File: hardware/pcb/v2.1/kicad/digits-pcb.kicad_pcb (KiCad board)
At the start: 2 copper layers, 61.9 x 76.2 mm, 77 parts, among them J1 Conn_02x20_Odd_Even, J3 VIN_BARREL_PIGTAIL, J4 Conn_01x07, J6 Conn_01x02, J7 Screw_Terminal_01x02, J8 Conn_01x04, SW1 Hook_DPDT, SW2 SW_Push, U10 XL6019E1, U2 DRV8871DDAR, U3 RP2040, U4 W25Q16JVSSIQ, U5 AMS1117-3.3, U6 TLV320AIC3104IRHBR, U7 XC6206P182MR, Y1 ABM8-272-T3

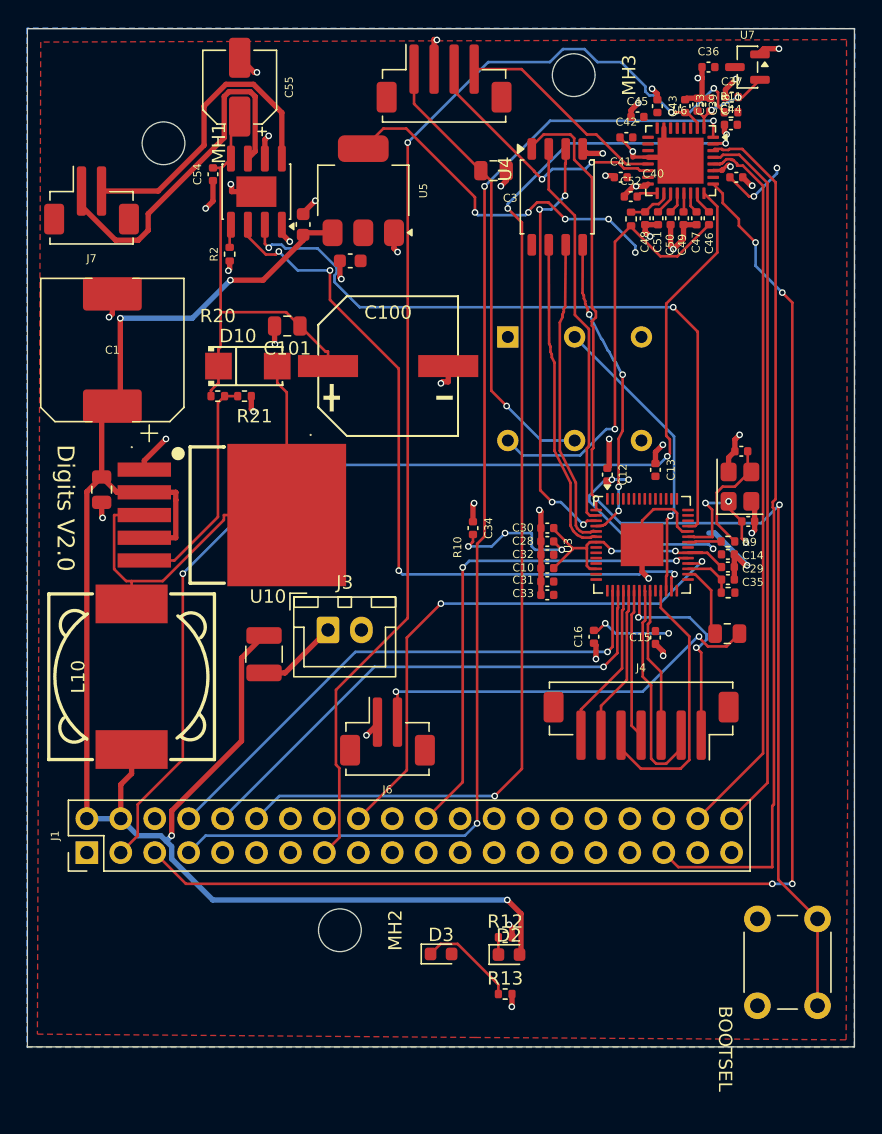
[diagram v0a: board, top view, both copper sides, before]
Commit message: fix(hardware): sync connector refs across sch/pcb, clean pre-fab defects
Rename connectors to semantic references in both schematic and PCB so the
two stay consistent: PWR, LED, KEYPAD, BELL, "Pi Zero W 2". Update the
baked unconnected-net placeholder names on the Pi header to match. Remove
a dangling via stub on the XIN crystal net, and add two GND vias to the
DRV8871 (U2) exposed pad for a lower-inductance ground tie.

DRC clean: 0 errors, 0 unconnected, 0 schematic-parity issues.
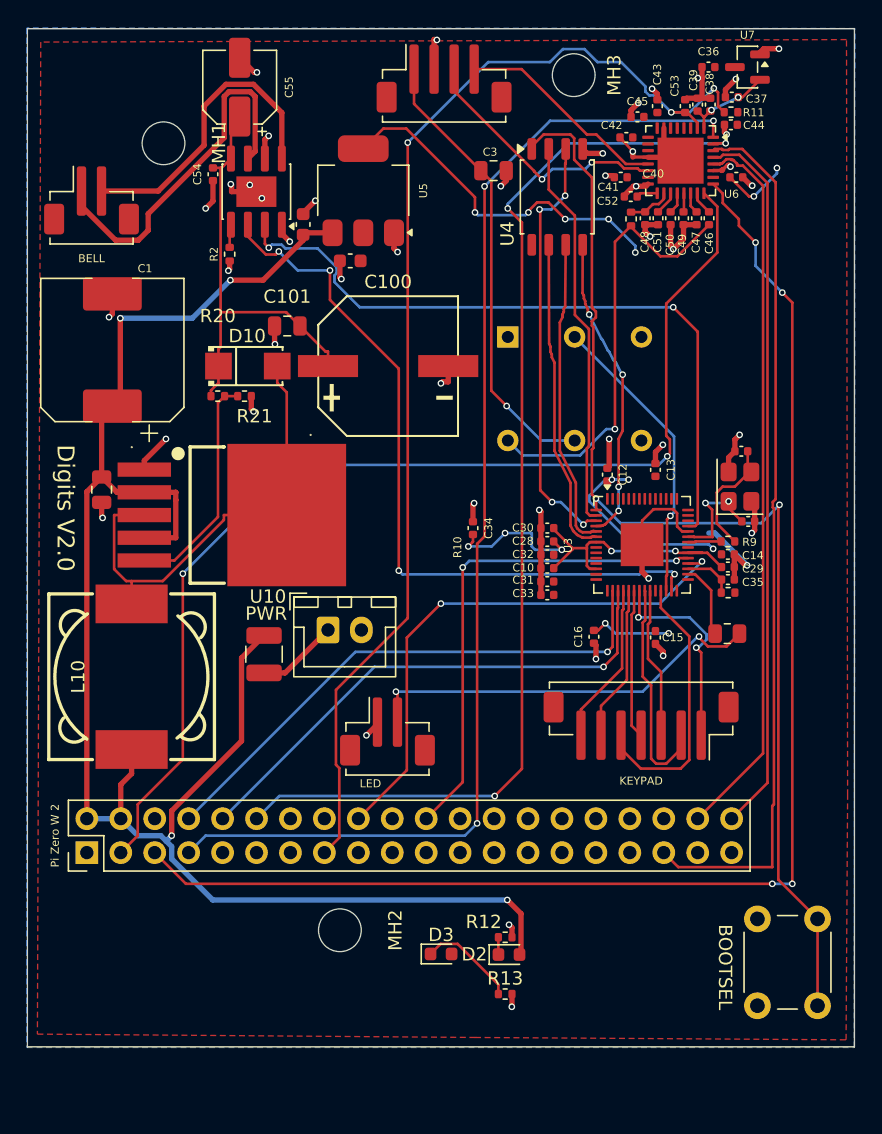
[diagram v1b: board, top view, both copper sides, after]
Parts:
- Pi Zero W 2: renamed from J1
- renumbered J7 to BELL, J4 to KEYPAD, J6 to LED, J3 to PWR
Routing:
- net XIN: track 10.0 -> 8.32 mm, vias 3 -> 2
- net GND: vias 44 -> 46
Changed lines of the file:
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@@
 		(tags "capacitor")
 		(property "Reference" "C41"
-			(at 0 1.16 0)
+			(at 0.934 -0.7327 0)
 			(layer "F.SilkS")
 			(effects
@@
 		(tags "capacitor electrolytic")
 		(property "Reference" "C1"
-			(at 0 0 0)
+			(at 6.0984 2.4411 0)
 			(layer "F.SilkS")
 			(effects
@@
 		(tags "capacitor")
 		(property "Reference" "C39"
-			(at 0 1.16 90)
+			(at 1.8319 -0.3115 90)
 			(layer "F.SilkS")
 			(effects
@@
 		(tags "capacitor")
 		(property "Reference" "C15"
-			(at 0 1.16 0)
+			(at 0 -1.2934 0)
 			(layer "F.SilkS")
 			(effects
@@
 		(tags "resistor")
 		(property "Reference" "R12"
-			(at 0 -1.17 0)
+			(at -1.61 -1.15 0)
 			(layer "F.SilkS")
 			(effects
@@
 		(tags "capacitor")
 		(property "Reference" "C101"
-			(at 0 -1.68 0)
+			(at 0 2.2 0)
 			(layer "F.SilkS")
 			(effects
@@
 		(tags "LED")
 		(property "Reference" "D2"
-			(at 0 -1.43 0)
+			(at -2.595 -0.02 0)
 			(layer "F.SilkS")
 			(effects
@@
 		(tags "capacitor")
 		(property "Reference" "C43"
-			(at 0 1.16 90)
+			(at 2.3696 -0.0021 90)
 			(layer "F.SilkS")
 			(effects
@@
 		(tags "mountinghole M3")
 		(property "Reference" "MH3"
-			(at 0 4.15 90)
+			(at 0 3.036 90)
 			(layer "F.SilkS")
 			(effects
@@
 		(tags "capacitor")
 		(property "Reference" "C44"
-			(at 0 1.16 0)
+			(at -1.7216 -0.0339 0)
 			(layer "F.SilkS")
 			(effects
@@
 		(tags "capacitor")
 		(property "Reference" "C42"
-			(at 0 1.16 0)
+			(at 1.1057 0.9148 0)
 			(layer "F.SilkS")
 			(effects
@@
 		(tags "Texas VQFN NoLead")
 		(property "Reference" "U6"
-			(at 0.0625 3.75 0)
+			(at -3.811 -2.4995 0)
 			(layer "F.SilkS")
 			(effects
@@
 		(tags "resistor")
 		(property "Reference" "R11"
-			(at 0 1.17 0)
+			(at -1.6879 -0.026 0)
 			(layer "F.SilkS")
 			(effects
@@
 		(descr "SS56")
 		(property "Reference" "D10"
-			(at -0.75 -2.25 0)
+			(at -0.05 -2.25 0)
 			(layer "F.SilkS")
 			(effects
@@
 		(tags "capacitor")
 		(property "Reference" "C3"
-			(at 1.25 2.05 0)
+			(at -0.264 -1.4005 0)
 			(layer "F.SilkS")
 			(effects
@@
 		(tags "SOIC SO P-SOP SOP SOP-8 SO SO-8 8S2 S2AE/F K04-056 CASE-751BE SO8W 8-Pin-SOIC PSA W8-2 W8-4 W8MS-1 FPT-8P-M08")
 		(property "Reference" "U4"
-			(at -2.0875 3.905 90)
+			(at 2.76 3.73 90)
 			(layer "F.SilkS")
 			(effects
@@
 		(descr "JST XH series connector, B2B-XH-A (http://www.jst-mfg.com/product/pdf/eng/eXH.pdf)")
 		(tags "connector JST XH vertical")
-		(property "Reference" "J3"
-			(at 1.25 -3.55 0)
+		(property "Reference" "PWR"
+			(at -4.625 -1.225 0)
 			(layer "F.SilkS")
 			(effects
@@
 		(tags "capacitor")
 		(property "Reference" "C53"
-			(at 0.112504 1.133301 90)
+			(at 1.5186 -0.7804 90)
 			(layer "F.SilkS")
 			(effects
@@
 		(tags "capacitor")
 		(property "Reference" "C38"
-			(at 0 1.16 90)
+			(at 1.5555 -0.0373 90)
 			(layer "F.SilkS")
 			(effects
@@
 		(descr "Through hole straight pin header, 2x20, 2.54mm pitch, double rows")
 		(tags "Through hole pin header THT 2x20 2.54mm double row")
-		(property "Reference" "J1"
+		(property "Reference" "Pi Zero W 2"
 			(at 1.27 -2.38 90)
 			(layer "F.SilkS")
@@
 			(layers "*.Cu" "*.Mask")
 			(remove_unused_layers no)
-			(net "unconnected-(J1-Pin_1-Pad1)")
+			(net "unconnected-(Pi Zero W 2-Pin_1-Pad1)")
 			(pinfunction "Pin_1_1")
 			(pintype "passive+no_connect")
@@
 			(layers "*.Cu" "*.Mask")
 			(remove_unused_layers no)
-			(net "unconnected-(J1-Pin_11-Pad11)")
+			(net "unconnected-(Pi Zero W 2-Pin_11-Pad11)")
 			(pinfunction "Pin_11_11")
 			(pintype "passive+no_connect")
@@
 			(layers "*.Cu" "*.Mask")
 			(remove_unused_layers no)
-			(net "unconnected-(J1-Pin_13-Pad13)")
+			(net "unconnected-(Pi Zero W 2-Pin_13-Pad13)")
 			(pinfunction "Pin_13_13")
 			(pintype "passive+no_connect")
@@
 			(layers "*.Cu" "*.Mask")
 			(remove_unused_layers no)
-			(net "unconnected-(J1-Pin_16-Pad16)")
+			(net "unconnected-(Pi Zero W 2-Pin_16-Pad16)")
 			(pinfunction "Pin_16_16")
 			(pintype "passive+no_connect")
@@
 			(layers "*.Cu" "*.Mask")
 			(remove_unused_layers no)
-			(net "unconnected-(J1-Pin_17-Pad17)")
+			(net "unconnected-(Pi Zero W 2-Pin_17-Pad17)")
 			(pinfunction "Pin_17_17")
 			(pintype "passive+no_connect")
@@
 			(layers "*.Cu" "*.Mask")
 			(remove_unused_layers no)
-			(net "unconnected-(J1-Pin_19-Pad19)")
+			(net "unconnected-(Pi Zero W 2-Pin_19-Pad19)")
 			(pinfunction "Pin_19_19")
 			(pintype "passive+no_connect")
@@
 			(layers "*.Cu" "*.Mask")
 			(remove_unused_layers no)
-			(net "unconnected-(J1-Pin_21-Pad21)")
+			(net "unconnected-(Pi Zero W 2-Pin_21-Pad21)")
 			(pinfunction "Pin_21_21")
 			(pintype "passive+no_connect")
@@
 			(layers "*.Cu" "*.Mask")
 			(remove_unused_layers no)
-			(net "unconnected-(J1-Pin_23-Pad23)")
+			(net "unconnected-(Pi Zero W 2-Pin_23-Pad23)")
 			(pinfunction "Pin_23_23")
 			(pintype "passive+no_connect")
@@
 			(layers "*.Cu" "*.Mask")
 			(remove_unused_layers no)
-			(net "unconnected-(J1-Pin_24-Pad24)")
+			(net "unconnected-(Pi Zero W 2-Pin_24-Pad24)")
 			(pinfunction "Pin_24_24")
 			(pintype "passive+no_connect")
@@
 			(layers "*.Cu" "*.Mask")
 			(remove_unused_layers no)
-			(net "unconnected-(J1-Pin_26-Pad26)")
+			(net "unconnected-(Pi Zero W 2-Pin_26-Pad26)")
 			(pinfunction "Pin_26_26")
 			(pintype "passive+no_connect")
@@
 			(layers "*.Cu" "*.Mask")
 			(remove_unused_layers no)
-			(net "unconnected-(J1-Pin_27-Pad27)")
+			(net "unconnected-(Pi Zero W 2-Pin_27-Pad27)")
 			(pinfunction "Pin_27_27")
 			(pintype "passive+no_connect")
@@
 			(layers "*.Cu" "*.Mask")
 			(remove_unused_layers no)
-			(net "unconnected-(J1-Pin_28-Pad28)")
+			(net "unconnected-(Pi Zero W 2-Pin_28-Pad28)")
 			(pinfunction "Pin_28_28")
 			(pintype "passive+no_connect")
@@
 			(layers "*.Cu" "*.Mask")
 			(remove_unused_layers no)
-			(net "unconnected-(J1-Pin_29-Pad29)")
+			(net "unconnected-(Pi Zero W 2-Pin_29-Pad29)")
 			(pinfunction "Pin_29_29")
 			(pintype "passive+no_connect")
@@
 			(layers "*.Cu" "*.Mask")
 			(remove_unused_layers no)
-			(net "unconnected-(J1-Pin_31-Pad31)")
+			(net "unconnected-(Pi Zero W 2-Pin_31-Pad31)")
 			(pinfunction "Pin_31_31")
 			(pintype "passive+no_connect")
@@
 			(layers "*.Cu" "*.Mask")
 			(remove_unused_layers no)
-			(net "unconnected-(J1-Pin_32-Pad32)")
+			(net "unconnected-(Pi Zero W 2-Pin_32-Pad32)")
 			(pinfunction "Pin_32_32")
 			(pintype "passive+no_connect")
@@
 			(layers "*.Cu" "*.Mask")
 			(remove_unused_layers no)
-			(net "unconnected-(J1-Pin_33-Pad33)")
+			(net "unconnected-(Pi Zero W 2-Pin_33-Pad33)")
 			(pinfunction "Pin_33_33")
 			(pintype "passive+no_connect")
@@
 			(layers "*.Cu" "*.Mask")
 			(remove_unused_layers no)
-			(net "unconnected-(J1-Pin_36-Pad36)")
+			(net "unconnected-(Pi Zero W 2-Pin_36-Pad36)")
 			(pinfunction "Pin_36_36")
 			(pintype "passive+no_connect")
@@
 			(layers "*.Cu" "*.Mask")
 			(remove_unused_layers no)
-			(net "unconnected-(J1-Pin_37-Pad37)")
+			(net "unconnected-(Pi Zero W 2-Pin_37-Pad37)")
 			(pinfunction "Pin_37_37")
 			(pintype "passive+no_connect")
@@
 		(descr "JST ZH series connector, B2B-ZR-SM4-TF (http://www.jst-mfg.com/product/pdf/eng/eZH.pdf)")
 		(tags "connector JST ZH vertical")
-		(property "Reference" "J7"
+		(property "Reference" "BELL"
 			(at 0 4.35 0)
 			(layer "F.SilkS")
@@
 		(descr "100uF 63V")
 		(property "Reference" "C100"
-			(at 0 -4 0)
+			(at 0 -6.3 0)
 			(layer "F.SilkS")
 			(effects
@@
 		(tags "capacitor")
 		(property "Reference" "C37"
-			(at 0 1.16 0)
+			(at -1.8521 -0.1276 180)
 			(layer "F.SilkS")
 			(effects
@@
 		(descr "JST ZH series connector, B7B-ZR-SM4-TF (http://www.jst-mfg.com/product/pdf/eng/eZH.pdf)")
 		(tags "connector JST ZH vertical")
-		(property "Reference" "J4"
-			(at 0 4.35 0)
+		(property "Reference" "KEYPAD"
+			(at 0 -4.1245 0)
 			(layer "F.SilkS")
 			(effects
@@
 		(descr "JST ZH series connector, B2B-ZR-SM4-TF (http://www.jst-mfg.com/product/pdf/eng/eZH.pdf)")
 		(tags "connector JST ZH vertical")
-		(property "Reference" "J6"
-			(at 0 4.35 0)
+		(property "Reference" "LED"
+			(at -1.275 3.9 0)
 			(layer "F.SilkS")
 			(effects
@@
 		(tags "capacitor")
 		(property "Reference" "C52"
-			(at 0 1.16 0)
+			(at 1.734 -0.337 0)
 			(layer "F.SilkS")
 			(effects
@@
 	)
 	(gr_text "BOOTSEL"
-		(at 64.388989 85.335455 270)
+		(at 64.388989 79.235 270)
 		(layer "F.SilkS")
 		(effects
@@
 	)
 	(via
+		(at 29.4 23.9)
+		(size 0.5)
+		(drill 0.3)
+		(layers "F.Cu" "B.Cu")
+		(net "GND")
+	)
+	(via
 		(at 27.9715 23.8454)
 		(size 0.5)
@@
 	)
 	(via
+		(at 30.3 24.9)
+		(size 0.5)
+		(drill 0.3)
+		(layers "F.Cu" "B.Cu")
+		(net "GND")
+	)
+	(via
 		(at 40.4572 28.9232)
 		(size 0.5)
@@
 	)
 	(segment
-		(start 66.2219 50.367)
-		(end 66.5308 50.6759)
-		(width 0.2)
-		(layer "F.Cu")
-		(net "XIN")
-	)
-	(segment
-		(start 66.2219 49.0855)
-		(end 66.2219 50.367)
-		(width 0.2)
-		(layer "F.Cu")
-		(net "XIN")
-	)
-	(segment
 		(start 65.2319 48.0955)
 		(end 66.2219 49.0855)
@@
 		(net "XIN")
 	)
-	(via
-		(at 66.5308 50.6759)
-		(size 0.5)
-		(drill 0.3)
-		(layers "F.Cu" "B.Cu")
-		(net "XIN")
-	)
